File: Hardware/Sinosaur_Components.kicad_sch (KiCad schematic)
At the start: 82 parts, among them J1 Conn_01x12_Male, J2 Conn_01x12_Male, J3 Conn_01x16_Male, J4 Conn_01x16_Male, J5 SWD_Header, J6 Eurorack_16_pin_power, J7 UART_Test_Pins, J8 USB_B_Micro, Q1 MMBT3904, Q2 MMBT3904, U1 STM32G473V, U2 STF202-22T1G, U3 TL074, U4 TL074, U5 LT1117-3.3, Y1 8MHz 20pF

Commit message: Gerber production
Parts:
- added TP6: TestPoint, Custom_Footprints:1mm_Test_Point, symbol Connector:TestPoint
- J1, J2, J3, J4, J5, J6, J7, TP1, TP2, TP3, TP4, TP5: now left out of the parts list
- U3, U4: footprint Package_SO:TSSOP-14_4.4x5mm_P0.65mm -> Package_SO:SOIC-14_3.9x8.7mm_P1.27mm
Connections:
- net GND: now also U4.10 (+), TP6.1; no longer U4.9 (-)
- net Sine3_DAC: now also U4.3 (+); no longer U4.2 (-)
- net Sine3_Swell_Rate: now also U1.10 (PF9); no longer U1.9 (PC15)
- net at R13.2, R17.2: now also U4.2 (-); no longer U4.3 (+)
- net at R10.1, R14.2: now also U4.9 (-); no longer U4.10 (+)
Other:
- note added: "Gain: 3.3 * (1 + 10k / 10k) = 6.6V Inverting: 3.3 * (-20k / 10k) = -6.6V"
- note removed: "Gain: 3.3 * (1 + 10k / 10k) = 6.6V Inverting: 3.3 * (20k / 10k) = -6.6V"
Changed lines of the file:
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@@
 	)
 	(no_connect
-		(at 53.34 78.74)
+		(at 99.06 167.64)
 	)
 	(no_connect
@@
 		)
 	)
-	(text "Gain: 3.3 * (1 + 10k / 10k) = 6.6V\nInverting: 3.3 * (20k / 10k) = -6.6V"
+	(text "Gain: 3.3 * (1 + 10k / 10k) = 6.6V\nInverting: 3.3 * (-20k / 10k) = -6.6V"
 		(exclude_from_sim no)
 		(at 189.738 180.34 0)
@@
 	)
 	(label "Sine3_Swell_Rate"
-		(at 99.06 167.64 0)
+		(at 53.34 78.74 180)
 		(fields_autoplaced yes)
 		(effects
@@
 				(size 1.27 1.27)
 			)
-			(justify left bottom)
+			(justify right bottom)
 		)
 	)
@@
 			)
 		)
-		(property "Footprint" "Package_SO:TSSOP-14_4.4x5mm_P0.65mm"
+		(property "Footprint" "Package_SO:SOIC-14_3.9x8.7mm_P1.27mm"
 			(at 149.86 27.94 0)
 			(effects
@@
 		(unit 1)
 		(exclude_from_sim no)
-		(in_bom yes)
+		(in_bom no)
 		(on_board yes)
 		(dnp no)
@@
 		(unit 1)
 		(exclude_from_sim no)
-		(in_bom yes)
+		(in_bom no)
 		(on_board yes)
 		(dnp no)
@@
 		(unit 1)
 		(exclude_from_sim no)
-		(in_bom yes)
+		(in_bom no)
 		(on_board yes)
 		(dnp no)
@@
 		(unit 1)
 		(exclude_from_sim no)
-		(in_bom yes)
+		(in_bom no)
 		(on_board yes)
 		(dnp no)
@@
 			)
 		)
-		(property "Footprint" "Package_SO:TSSOP-14_4.4x5mm_P0.65mm"
+		(property "Footprint" "Package_SO:SOIC-14_3.9x8.7mm_P1.27mm"
 			(at 149.86 134.62 0)
 			(effects
@@
 		)
 		(property "Value" "GND"
-			(at 344.932 111.252 90)
+			(at 344.678 110.998 90)
 			(effects
 				(font
@@
 		(unit 1)
 		(exclude_from_sim no)
-		(in_bom yes)
+		(in_bom no)
 		(on_board yes)
 		(dnp no)
@@
 		(unit 1)
 		(exclude_from_sim no)
-		(in_bom yes)
+		(in_bom no)
 		(on_board yes)
 		(dnp no)
@@
 			)
 		)
-		(property "Footprint" "Package_SO:TSSOP-14_4.4x5mm_P0.65mm"
+		(property "Footprint" "Package_SO:SOIC-14_3.9x8.7mm_P1.27mm"
 			(at 203.2 62.23 0)
 			(effects
@@
 			)
 		)
-		(property "Footprint" "Package_SO:TSSOP-14_4.4x5mm_P0.65mm"
+		(property "Footprint" "Package_SO:SOIC-14_3.9x8.7mm_P1.27mm"
 			(at 149.86 62.23 0)
 			(effects
@@
 		(unit 1)
 		(exclude_from_sim no)
-		(in_bom yes)
+		(in_bom no)
 		(on_board yes)
 		(dnp no)
@@
 			)
 		)
-		(property "Footprint" "Package_SO:TSSOP-14_4.4x5mm_P0.65mm"
+		(property "Footprint" "Package_SO:SOIC-14_3.9x8.7mm_P1.27mm"
 			(at 152.4 210.82 0)
 			(effects
@@
 		(unit 1)
 		(exclude_from_sim no)
-		(in_bom yes)
+		(in_bom no)
 		(on_board yes)
 		(dnp no)
@@
 	)
 	(symbol
+		(lib_id "power:GND")
+		(at 210.82 209.55 90)
+		(unit 1)
+		(exclude_from_sim no)
+		(in_bom yes)
+		(on_board yes)
+		(dnp no)
+		(property "Reference" "#PWR054"
+			(at 217.17 209.55 0)
+			(effects
+				(font
+					(size 1.27 1.27)
+				)
+				(hide yes)
+			)
+		)
+		(property "Value" "GND"
+			(at 214.63 209.55 90)
+			(effects
+				(font
+					(size 1.27 1.27)
+				)
+				(justify right)
+			)
+		)
+		(property "Footprint" ""
+			(at 210.82 209.55 0)
+			(effects
+				(font
+					(size 1.27 1.27)
+				)
+				(hide yes)
+			)
+		)
+		(property "Datasheet" ""
+			(at 210.82 209.55 0)
+			(effects
+				(font
+					(size 1.27 1.27)
+				)
+				(hide yes)
+			)
+		)
+		(property "Description" "Power symbol creates a global label with name \"GND\" , ground"
+			(at 210.82 209.55 0)
+			(effects
+				(font
+					(size 1.27 1.27)
+				)
+				(hide yes)
+			)
+		)
+		(pin "1"
+		)
+		(instances
+			(project "Sinosaur_Components"
+				(path "/ea88d275-24e2-4917-9451-7e51068364d9"
+					(reference "#PWR054")
+					(unit 1)
+				)
+			)
+		)
+	)
+	(symbol
 		(lib_id "power:+12V")
 		(at 209.55 226.06 270)
@@
 		(unit 1)
 		(exclude_from_sim no)
-		(in_bom yes)
+		(in_bom no)
 		(on_board yes)
 		(dnp no)
@@
 		(lib_id "Amplifier_Operational:TL074")
 		(at 204.47 144.78 0)
+		(mirror x)
 		(unit 3)
 		(exclude_from_sim no)
@@
 		(on_board yes)
 		(dnp no)
+		(fields_autoplaced yes)
 		(property "Reference" "U4"
-			(at 204.47 135.4582 0)
+			(at 204.47 152.4 0)
 			(effects
 				(font
@@
 		)
 		(property "Value" "TL074"
-			(at 204.47 137.7696 0)
+			(at 204.47 154.94 0)
 			(effects
 				(font
@@
 			)
 		)
-		(property "Footprint" "Package_SO:TSSOP-14_4.4x5mm_P0.65mm"
-			(at 203.2 142.24 0)
+		(property "Footprint" "Package_SO:SOIC-14_3.9x8.7mm_P1.27mm"
+			(at 203.2 147.32 0)
 			(effects
 				(font
@@
 		)
 		(property "Datasheet" "http://www.ti.com/lit/ds/symlink/tl071.pdf"
-			(at 205.74 139.7 0)
+			(at 205.74 149.86 0)
 			(effects
 				(font
@@
 		(unit 1)
 		(exclude_from_sim no)
-		(in_bom yes)
+		(in_bom no)
 		(on_board yes)
 		(dnp no)
@@
 			)
 		)
-		(property "Footprint" "Package_SO:TSSOP-14_4.4x5mm_P0.65mm"
+		(property "Footprint" "Package_SO:SOIC-14_3.9x8.7mm_P1.27mm"
 			(at 176.53 210.82 0)
 			(effects
@@
 		(unit 1)
 		(exclude_from_sim no)
-		(in_bom yes)
+		(in_bom no)
 		(on_board yes)
 		(dnp no)
@@
 			)
 		)
-		(property "Footprint" "Package_SO:TSSOP-14_4.4x5mm_P0.65mm"
+		(property "Footprint" "Package_SO:SOIC-14_3.9x8.7mm_P1.27mm"
 			(at 203.2 27.94 0)
 			(effects
@@
 			)
 		)
-		(property "Footprint" "Package_SO:TSSOP-14_4.4x5mm_P0.65mm"
+		(property "Footprint" "Package_SO:SOIC-14_3.9x8.7mm_P1.27mm"
 			(at 149.86 97.79 0)
 			(effects
@@
 		(unit 1)
 		(exclude_from_sim no)
-		(in_bom yes)
+		(in_bom no)
 		(on_board yes)
 		(dnp no)
@@
 	)
 	(symbol
+		(lib_id "Connector:TestPoint")
+		(at 210.82 209.55 90)
+		(mirror x)
+		(unit 1)
+		(exclude_from_sim no)
+		(in_bom no)
+		(on_board yes)
+		(dnp no)
+		(property "Reference" "TP6"
+			(at 205.74 209.5499 90)
+			(effects
+				(font
+					(size 1.27 1.27)
+				)
+				(justify left)
+			)
+		)
+		(property "Value" "TestPoint"
+			(at 201.93 209.55 90)
+			(effects
+				(font
+					(size 1.27 1.27)
+				)
+				(justify left)
+			)
+		)
+		(property "Footprint" "Custom_Footprints:1mm_Test_Point"
+			(at 210.82 214.63 0)
+			(effects
+				(font
+					(size 1.27 1.27)
+				)
+				(hide yes)
+			)
+		)
+		(property "Datasheet" "~"
+			(at 210.82 214.63 0)
+			(effects
+				(font
+					(size 1.27 1.27)
+				)
+				(hide yes)
+			)
+		)
+		(property "Description" "test point"
+			(at 210.82 209.55 0)
+			(effects
+				(font
+					(size 1.27 1.27)
+				)
+				(hide yes)
+			)
+		)
+		(pin "1"
+		)
+		(instances
+			(project "Sinosaur_Components"
+				(path "/ea88d275-24e2-4917-9451-7e51068364d9"
+					(reference "TP6")
+					(unit 1)
+				)
+			)
+		)
+	)
+	(symbol
 		(lib_id "power:GND")
 		(at 194.31 45.72 0)
@@
 		(lib_id "Amplifier_Operational:TL074")
 		(at 204.47 100.33 0)
-		(mirror x)
 		(unit 1)
 		(exclude_from_sim no)
@@
 			)
 		)
-		(property "Footprint" "Package_SO:TSSOP-14_4.4x5mm_P0.65mm"
-			(at 203.2 102.87 0)
+		(property "Footprint" "Package_SO:SOIC-14_3.9x8.7mm_P1.27mm"
+			(at 203.2 97.79 0)
 			(effects
 				(font
@@
 		)
 		(property "Datasheet" "http://www.ti.com/lit/ds/symlink/tl071.pdf"
-			(at 205.74 105.41 0)
+			(at 205.74 95.25 0)
 			(effects
 				(font

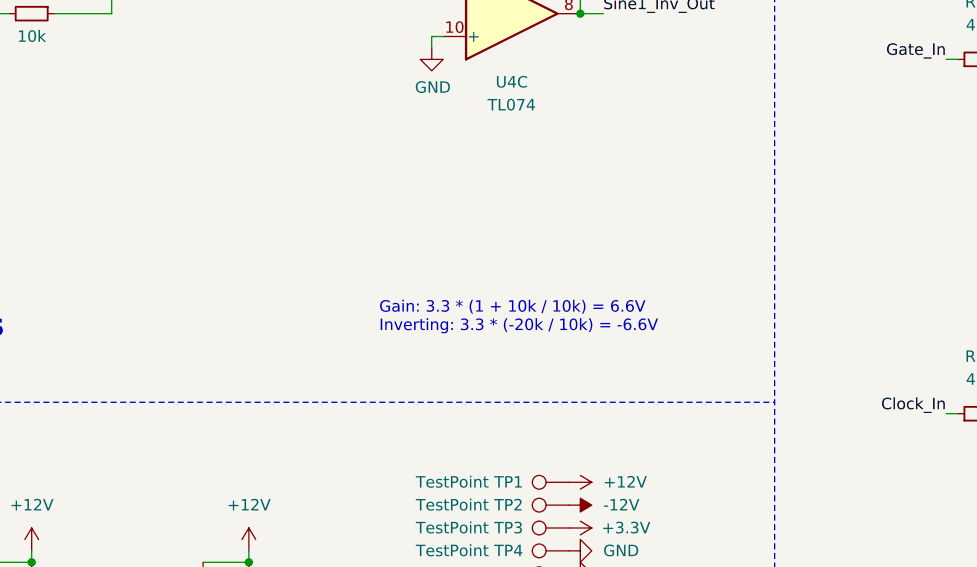
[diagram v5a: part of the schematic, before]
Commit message: Hardware working; started adding modulation code
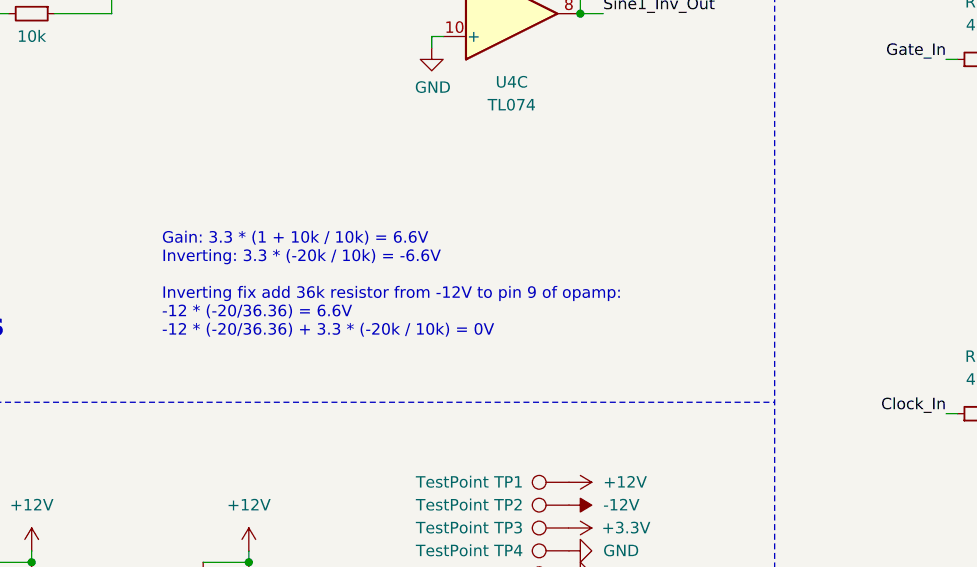
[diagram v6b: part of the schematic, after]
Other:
- note added: "Gain: 3.3 * (1 + 10k / 10k) = 6.6V Inverting: 3.3 * (-20k / 10k) = -6.6V Inverting fix add 36k resistor from -12V to pin 9 of opamp: -12 * (-20/36.36) = 6.6V -12 * (-20/36.36) + 3.3 * (-20k / 10k) = 0V"
- note removed: "Gain: 3.3 * (1 + 10k / 10k) = 6.6V Inverting: 3.3 * (-20k / 10k) = -6.6V"
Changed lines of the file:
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@@
 		)
 	)
-	(text "Gain: 3.3 * (1 + 10k / 10k) = 6.6V\nInverting: 3.3 * (-20k / 10k) = -6.6V"
+	(text "Gain: 3.3 * (1 + 10k / 10k) = 6.6V\nInverting: 3.3 * (-20k / 10k) = -6.6V\n\nInverting fix add 36k resistor from -12V to pin 9 of opamp:\n-12 * (-20/36.36) = 6.6V\n-12 * (-20/36.36) + 3.3 * (-20k / 10k) = 0V"
 		(exclude_from_sim no)
-		(at 189.738 180.34 0)
+		(at 165.608 180.848 0)
 		(effects
 			(font

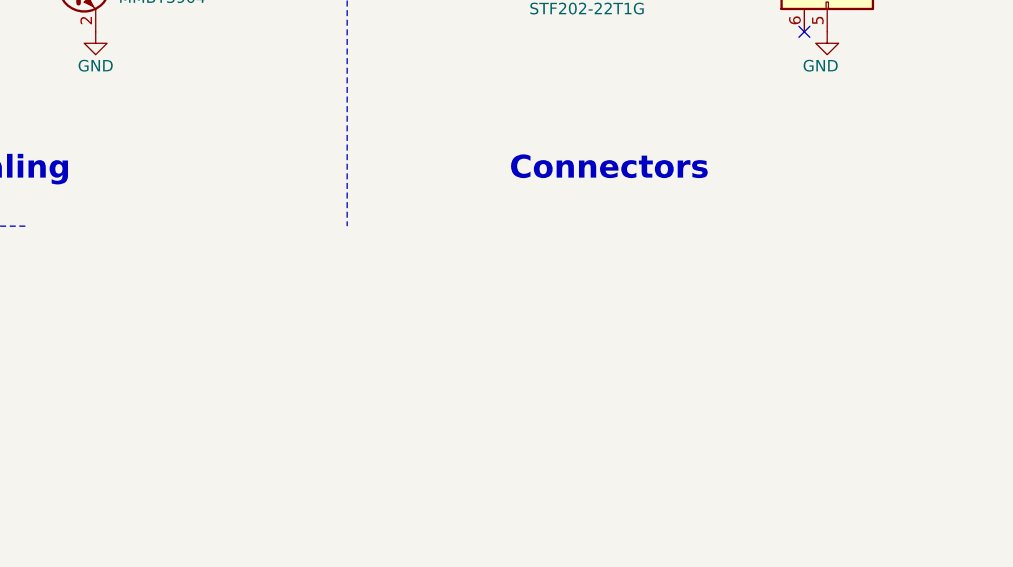
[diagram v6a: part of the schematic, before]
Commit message: Added REadme; code cleanup
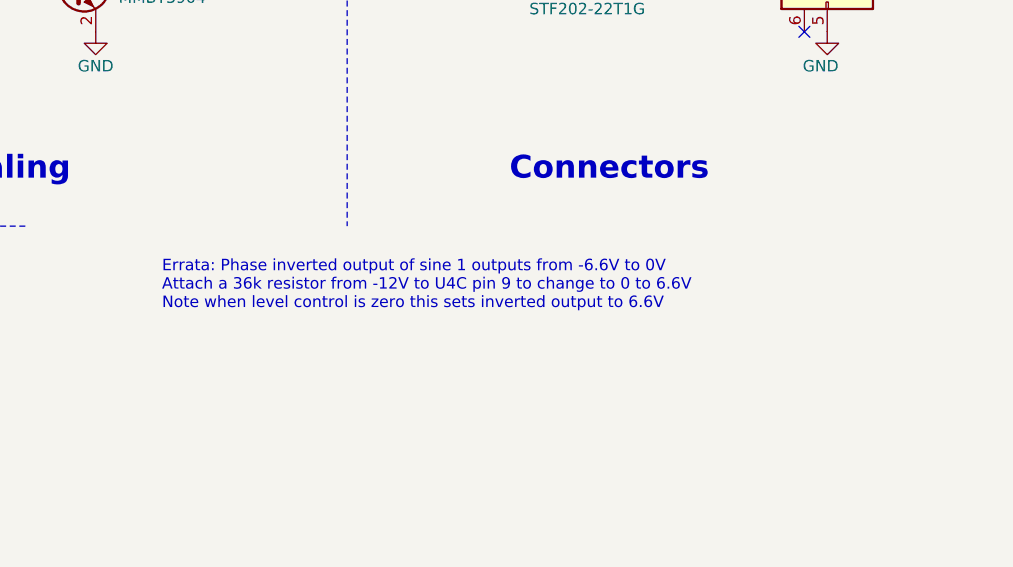
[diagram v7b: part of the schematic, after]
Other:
- note added: "Errata: Phase inverted output of sine 1 outputs from -6.6V to 0V Attach a 36k resistor from -12V to U4C pin 9 to change to 0 to 6.6V Note when level control is zero this sets inverted output to 6.6V"
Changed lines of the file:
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@@
+		)
+	)
+	(text "Errata: Phase inverted output of sine 1 outputs from -6.6V to 0V\nAttach a 36k resistor from -12V to U4C pin 9 to change to 0 to 6.6V\nNote when level control is zero this sets inverted output to 6.6V"
+		(exclude_from_sim no)
+		(at 274.066 222.504 0)
+		(effects
+			(font
+				(size 1.27 1.27)
+			)
+			(justify left)
 		)
 	)
